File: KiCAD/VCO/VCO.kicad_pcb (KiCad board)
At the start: 2 copper layers, 50 x 100 mm, 41 parts, among them J1 CV IN 1, J2 CV IN 2, J3 PWM, J4 SAW OUT, J5 PULSE OUT, J6 Conn_01x03_Pin, J7 Conn_01x03_Pin, Q1 NPN, T1 PNP, T2 NPN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

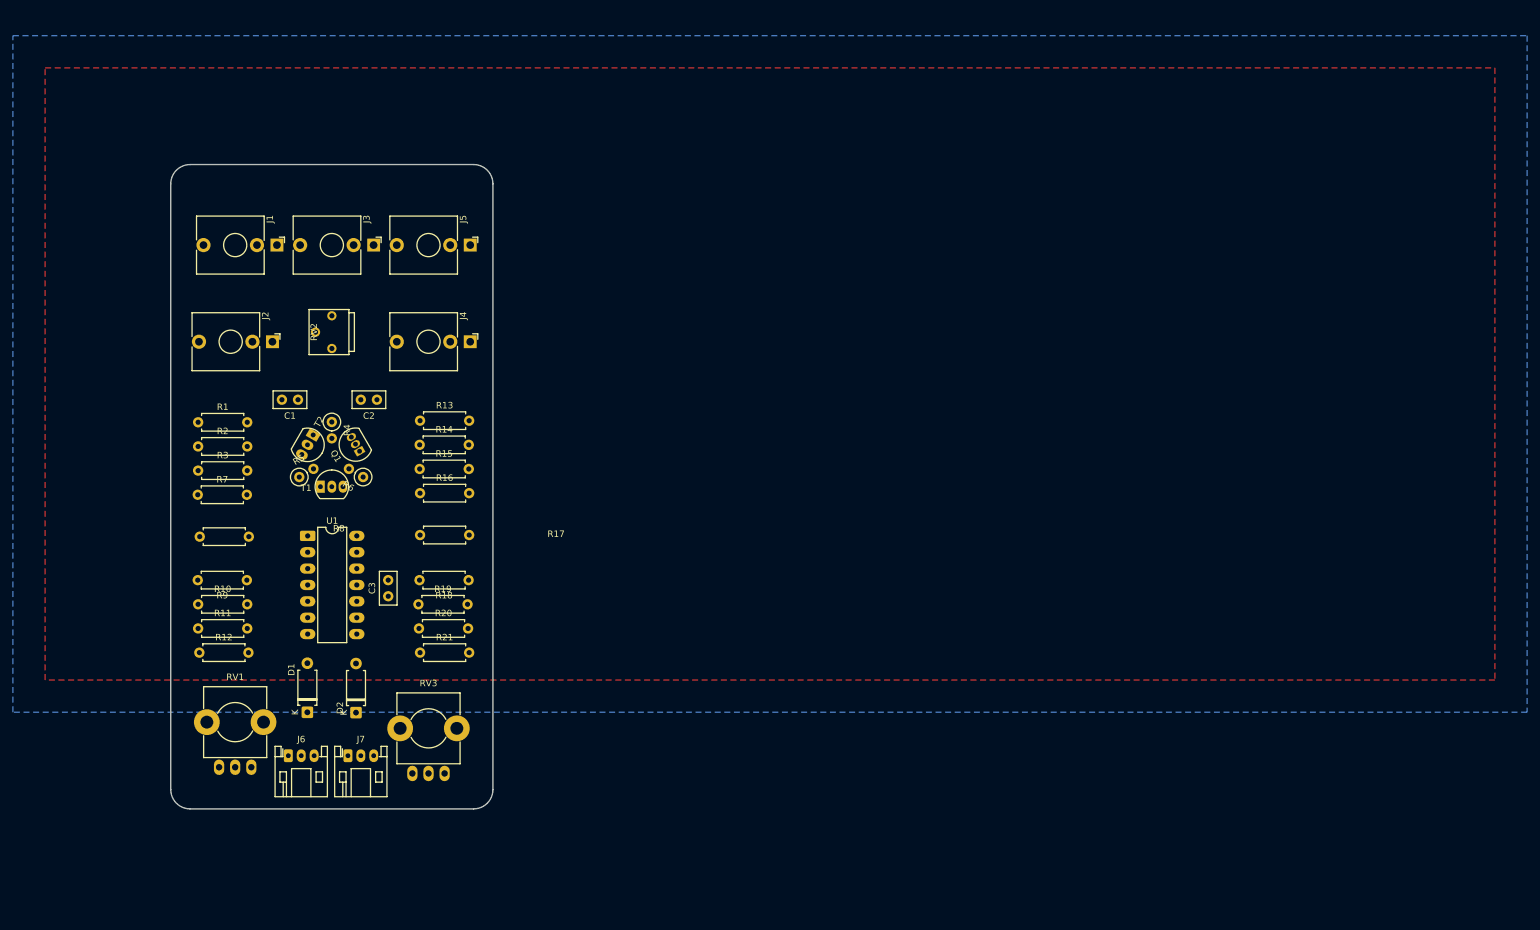
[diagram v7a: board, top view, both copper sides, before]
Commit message: Make the transistors touch
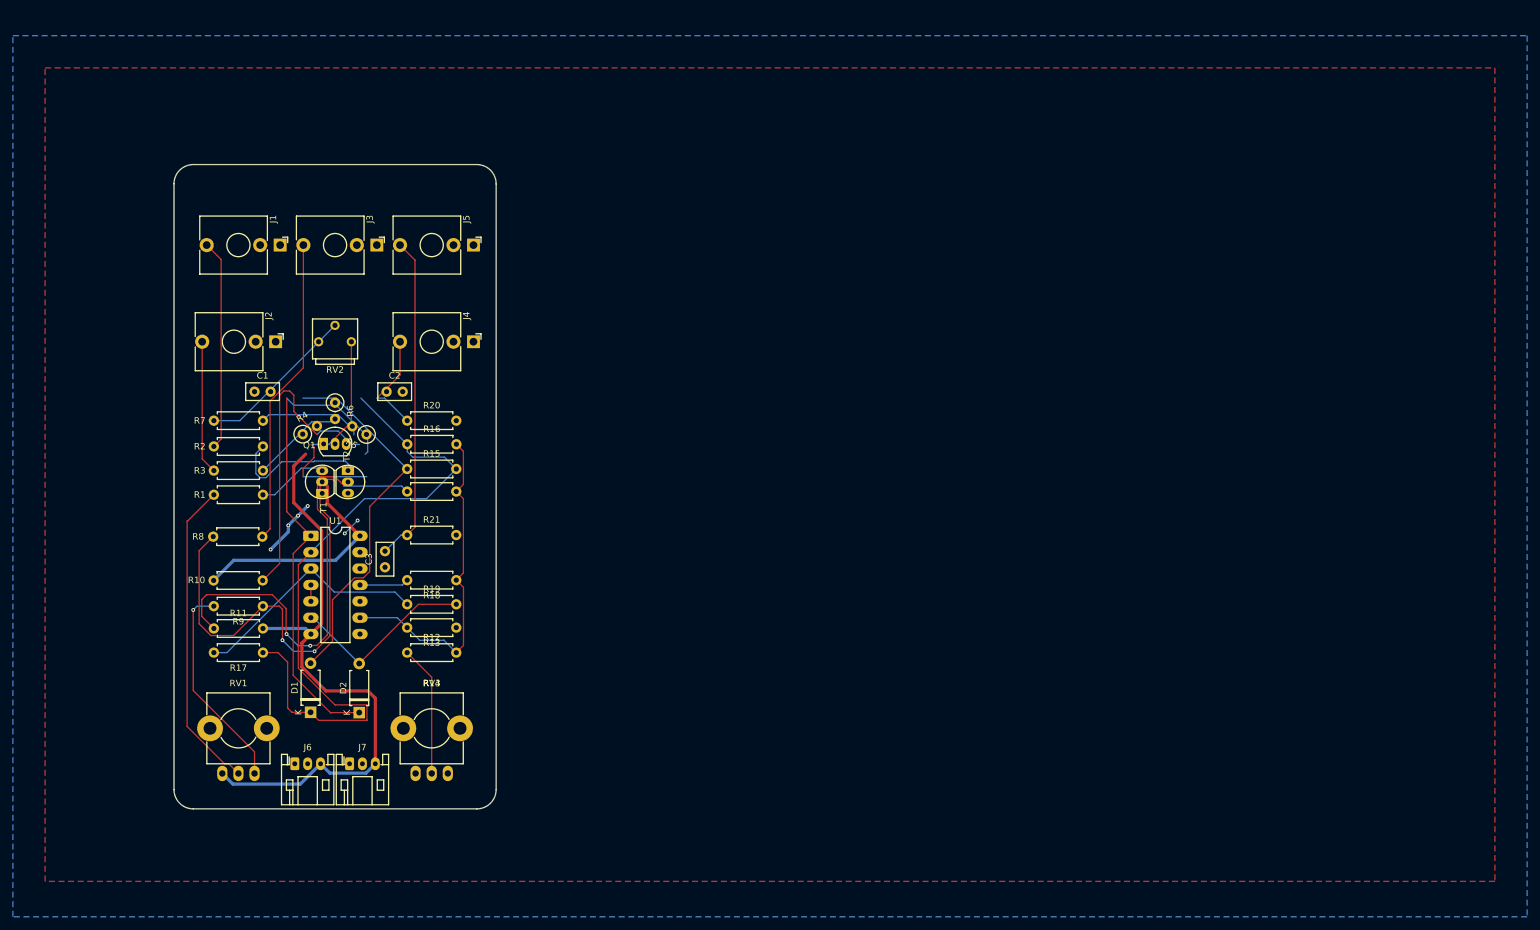
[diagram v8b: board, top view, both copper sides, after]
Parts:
- Q1: footprint Package_TO_SOT_THT:TO-92L_Inline -> HackSynth:TO-92_Inline - Handsolder
- moved R17 36.8 mm to (63.8, 125.8)
- moved R13 32.6 mm to (93.8, 121.9), turned to 180 degrees
- moved R20 32.3 mm to (86.2, 89.8)
- moved R12 32.2 mm to (86.2, 125.8)
- moved R21 18.4 mm to (86.2, 107.5)
- moved R5 12.3 mm to (79.9, 91.9), turned to 150 degrees
- moved R6 12.3 mm to (75.0, 87.0), turned to -90 degrees
- moved R7 11.8 mm to (56.2, 89.8)
- moved R1 11.5 mm to (56.2, 101.2)
- moved T2 7.95 mm to (77.0, 98.0), turned to -90 degrees
- moved R16 7.84 mm to (86.2, 93.4)
- moved R14 7.51 mm to (86.2, 100.8)
- moved C1 6.86 mm to (62.5, 85.2), turned to 0 degrees
- moved Q1 5.20 mm to (73.7, 93.4), turned to 0 degrees
- moved R4 4.89 mm to (70.0, 91.8), turned to 30 degrees
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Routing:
- net Net-(D1-K): track 0.00 -> 106.8 mm
- net VSS: track 0.00 -> 95.2 mm
- net Net-(Q1-E): track 0.00 -> 78.9 mm, vias 0 -> 2
- net Net-(Q1-B): track 0.00 -> 72.0 mm, vias 0 -> 2
- net Net-(D2-K): track 0.00 -> 58.4 mm
- net GND: track 0.00 -> 58.0 mm, vias 0 -> 6
- net Net-(D1-A): track 0.00 -> 57.9 mm
- net Net-(R12-Pad2): track 0.00 -> 52.3 mm
- net Net-(C3-Pad2): track 0.00 -> 50.9 mm
- net Net-(R1-Pad1): track 0.00 -> 48.7 mm
- net Net-(J3-PadT): track 0.00 -> 47.9 mm
- net Net-(T1-B): track 0.00 -> 43.9 mm
- net Net-(T1-C): track 0.00 -> 40.2 mm
- net VDD: track 0.00 -> 38.2 mm, vias 0 -> 1
- net Net-(R17-Pad2): track 0.00 -> 37.7 mm
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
